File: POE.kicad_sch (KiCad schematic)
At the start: 34 parts, among them J3 7466003R, J5 7466003R, Q1 FDS2582, T1 PA2369NL, U13 VO615A, U14 TL431PK, U3 NCP1081

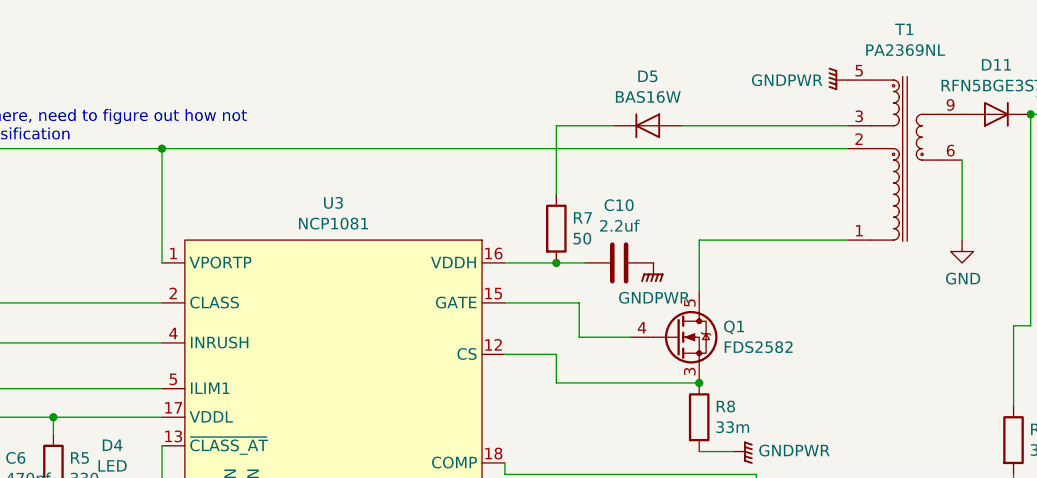
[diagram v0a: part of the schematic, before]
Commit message: Add transformer snubber diode
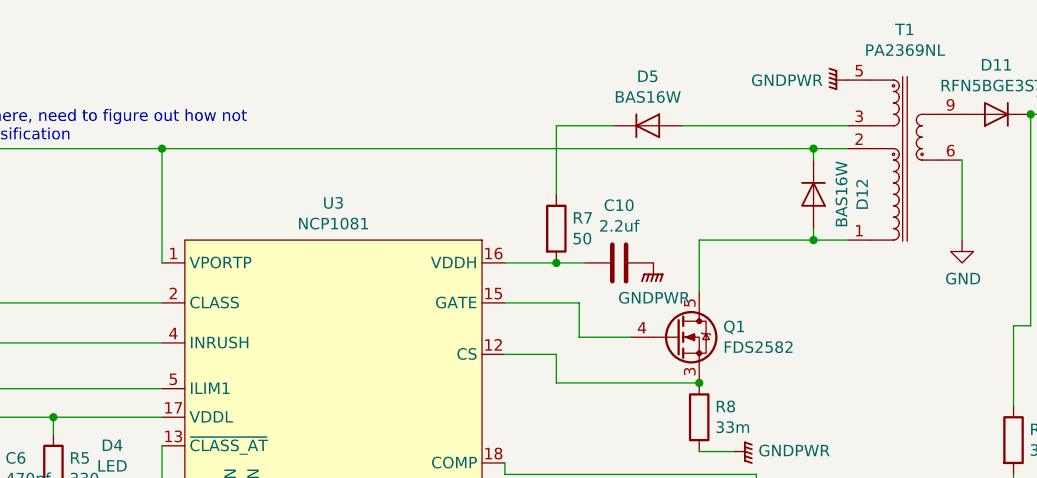
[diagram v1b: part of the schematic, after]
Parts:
- added D12: BAS16W, Package_TO_SOT_SMD:SOT-323_SC-70, symbol Diode:BAS16W
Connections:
- net POE_P: now also D12.3 (K)
- net at Q1.5 (D), Q1.6 (D), Q1.7 (D)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: now also D12.1 (A)
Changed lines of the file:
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@@
   (junction (at 182.88 85.09) (diameter 0) (color 0 0 0 0))
   (junction (at 182.88 92.71) (diameter 0) (color 0 0 0 0))
+  (junction (at 189.23 43.815) (diameter 0) (color 0 0 0 0))
+  (junction (at 189.23 53.975) (diameter 0) (color 0 0 0 0))
   (junction (at 213.36 40.005) (diameter 0) (color 0 0 0 0))
   (junction (at 217.805 40.005) (diameter 0) (color 0 0 0 0))
@@
     (stroke (width 0) (type solid) (color 0 0 0 0))
   )
-  (wire (pts (xy 116.84 43.815) (xy 193.04 43.815))
+  (wire (pts (xy 116.84 43.815) (xy 189.23 43.815))
     (stroke (width 0) (type solid) (color 0 0 0 0))
   )
@@
     (stroke (width 0) (type solid) (color 0 0 0 0))
   )
-  (wire (pts (xy 176.53 53.975) (xy 193.04 53.975))
+  (wire (pts (xy 176.53 53.975) (xy 189.23 53.975))
     (stroke (width 0) (type solid) (color 0 0 0 0))
   )
@@
   )
   (wire (pts (xy 182.88 92.71) (xy 191.77 92.71))
+    (stroke (width 0) (type solid) (color 0 0 0 0))
+  )
+  (wire (pts (xy 189.23 43.815) (xy 189.23 45.085))
+    (stroke (width 0) (type solid) (color 0 0 0 0))
+  )
+  (wire (pts (xy 189.23 43.815) (xy 193.04 43.815))
+    (stroke (width 0) (type solid) (color 0 0 0 0))
+  )
+  (wire (pts (xy 189.23 52.705) (xy 189.23 53.975))
+    (stroke (width 0) (type solid) (color 0 0 0 0))
+  )
+  (wire (pts (xy 189.23 53.975) (xy 193.04 53.975))
     (stroke (width 0) (type solid) (color 0 0 0 0))
   )
@@
       (effects (font (size 1.27 1.27)) hide)
     )
+  )
+  (symbol (lib_id "Diode:BAS16W") (at 189.23 48.895 270) (unit 1)
+    (in_bom yes) (on_board yes)
+    (property "Reference" "D12" (id 0) (at 194.6848 48.895 0))
+    (property "Value" "BAS16W" (id 1) (at 192.3861 48.895 0))
+    (property "Footprint" "Package_TO_SOT_SMD:SOT-323_SC-70" (id 2) (at 184.785 48.895 0)
+      (effects (font (size 1.27 1.27)) hide)
+    )
+    (property "Datasheet" "https://assets.nexperia.com/documents/data-sheet/BAS16_SER.pdf" (id 3) (at 189.23 48.895 0)
+      (effects (font (size 1.27 1.27)) hide)
+    )
